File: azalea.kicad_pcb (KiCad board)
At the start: 4 copper layers, 70.6 x 53.3 mm, 103 parts, among them J1 NEIGHBOR1, J2 NEIGHBOR2, J3 USB-MICRO-B-SHIELDED, J4 USB-MICRO-B-SHIELDED, J5 JTAG, J6 POWER, J7 BONUS_ROW, SW1 DFU, SW2 RESET, U1 LPC4330FBD144, U2 W25Q16DV, U3 AP7333, U4 IP4220CZ6, U5 AP2553W6-7, X1 MCU_XTAL, X2 RTC_XTAL

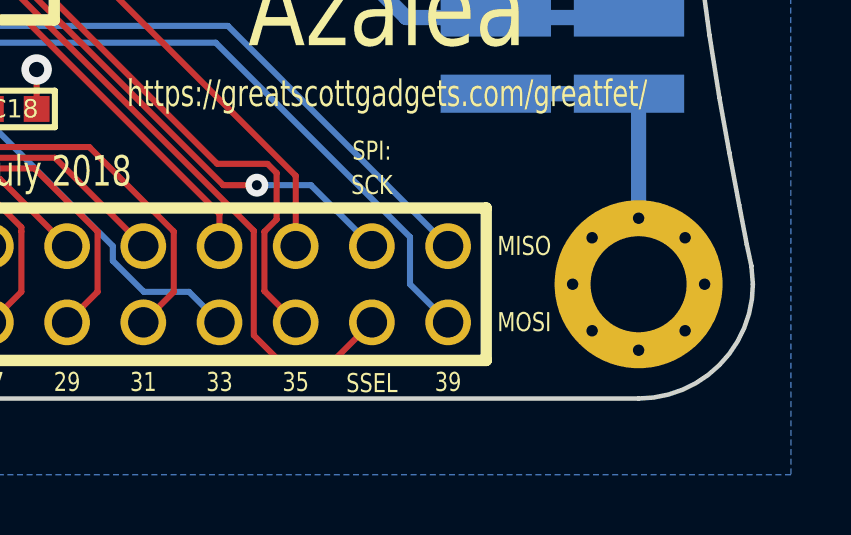
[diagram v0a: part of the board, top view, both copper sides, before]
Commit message: adopt OSHWA convention for SPI signal names https://www.oshwa.org/a-resolution-to-redefine-spi-signal-names
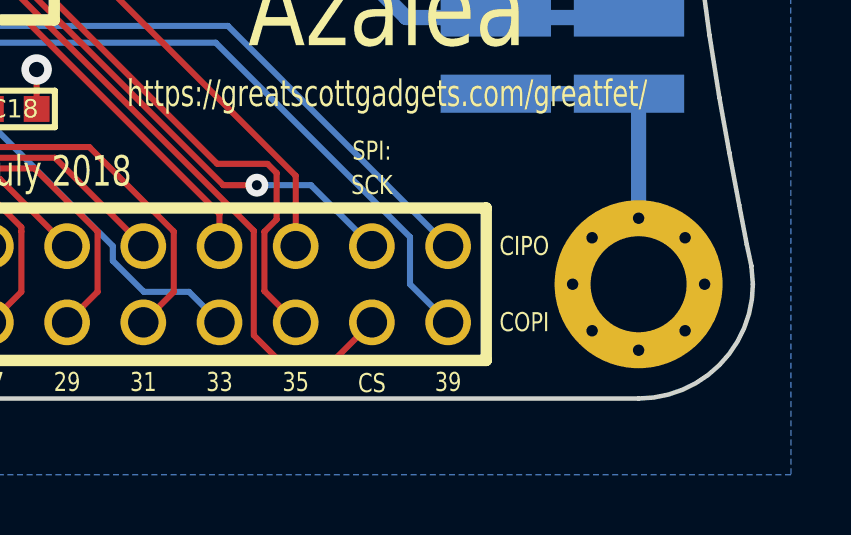
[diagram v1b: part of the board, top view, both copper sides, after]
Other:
- board text added: "CIPO"
- board text added: "COPI"
- board text added: "CS"
- board text removed: "MISO"
- board text removed: "MOSI"
- board text removed: "SSEL"
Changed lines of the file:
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@@
     (effects (font (size 0.635 0.508) (thickness 0.1016)) (justify mirror))
   )
-  (gr_text MOSI (at 168.91 121.92) (layer B.SilkS)
-    (effects (font (size 0.635 0.508) (thickness 0.1016)) (justify mirror))
-  )
-  (gr_text MISO (at 168.91 119.38) (layer B.SilkS)
+  (gr_text COPI (at 168.91 121.92) (layer B.SilkS)
+    (effects (font (size 0.635 0.508) (thickness 0.1016)) (justify mirror))
+  )
+  (gr_text CIPO (at 168.91 119.38) (layer B.SilkS)
     (effects (font (size 0.635 0.508) (thickness 0.1016)) (justify mirror))
   )
@@
     (effects (font (size 0.635 0.508) (thickness 0.1016)) (justify mirror))
   )
-  (gr_text SSEL (at 163.83 123.952) (layer B.SilkS)
+  (gr_text CS (at 163.83 123.952) (layer B.SilkS)
     (effects (font (size 0.635 0.508) (thickness 0.1016)) (justify mirror))
   )
@@
     (effects (font (size 0.635 0.508) (thickness 0.1016)))
   )
-  (gr_text SSEL (at 163.83 123.952) (layer F.SilkS)
-    (effects (font (size 0.635 0.508) (thickness 0.1016)))
-  )
-  (gr_text MISO (at 168.91 119.38) (layer F.SilkS)
-    (effects (font (size 0.635 0.508) (thickness 0.1016)))
-  )
-  (gr_text MOSI (at 168.91 121.92) (layer F.SilkS)
-    (effects (font (size 0.635 0.508) (thickness 0.1016)))
-  )
+  (gr_text CS (at 163.83 123.952) (layer F.SilkS)
+    (effects (font (size 0.635 0.508) (thickness 0.1016)))
+  )
+  (gr_text CIPO (at 168.91 119.38) (layer F.SilkS)
+    (effects (font (size 0.635 0.508) (thickness 0.1016)))
+  )
+  (gr_text COPI (at 168.91 121.92) (layer F.SilkS)
+    (effects (font (size 0.635 0.508) (thickness 0.1016)))
+  )

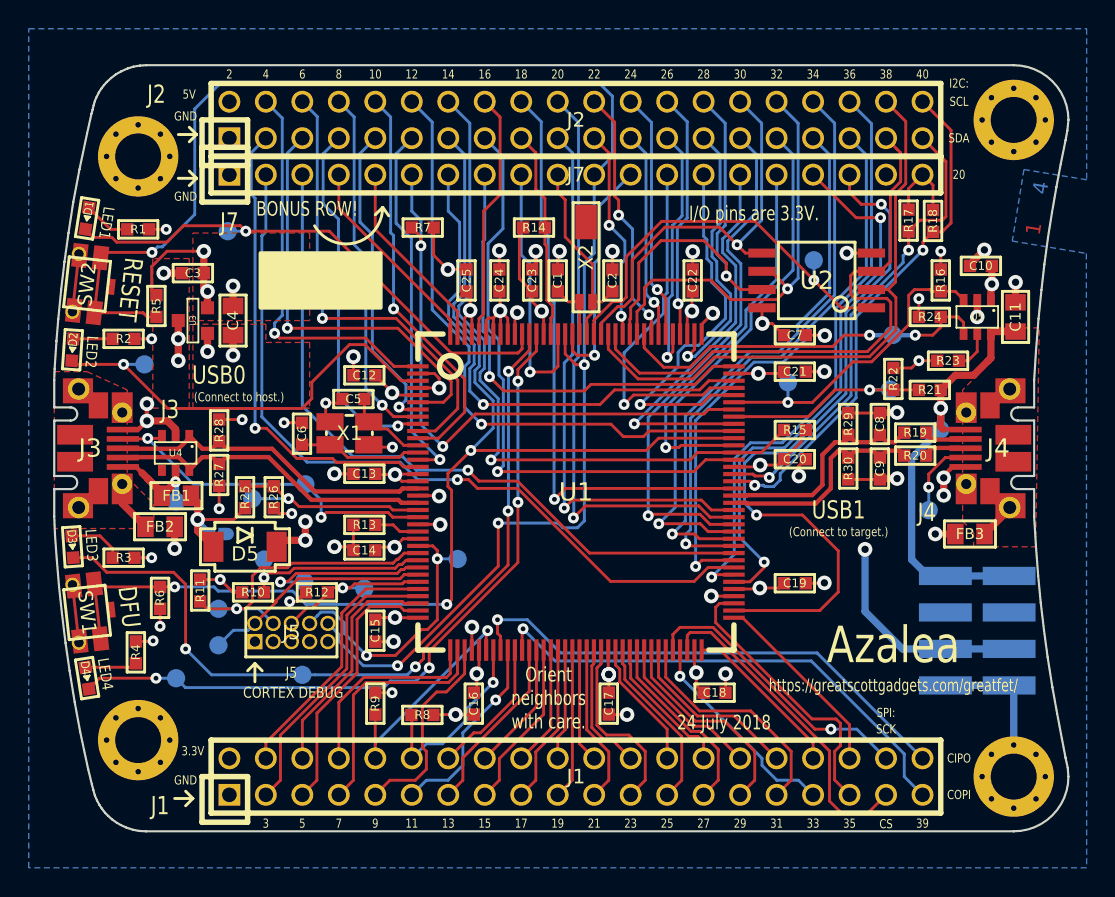
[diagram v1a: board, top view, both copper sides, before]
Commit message: GF1 hardware: Update PCB to reflect U5 & R23 peart changes.
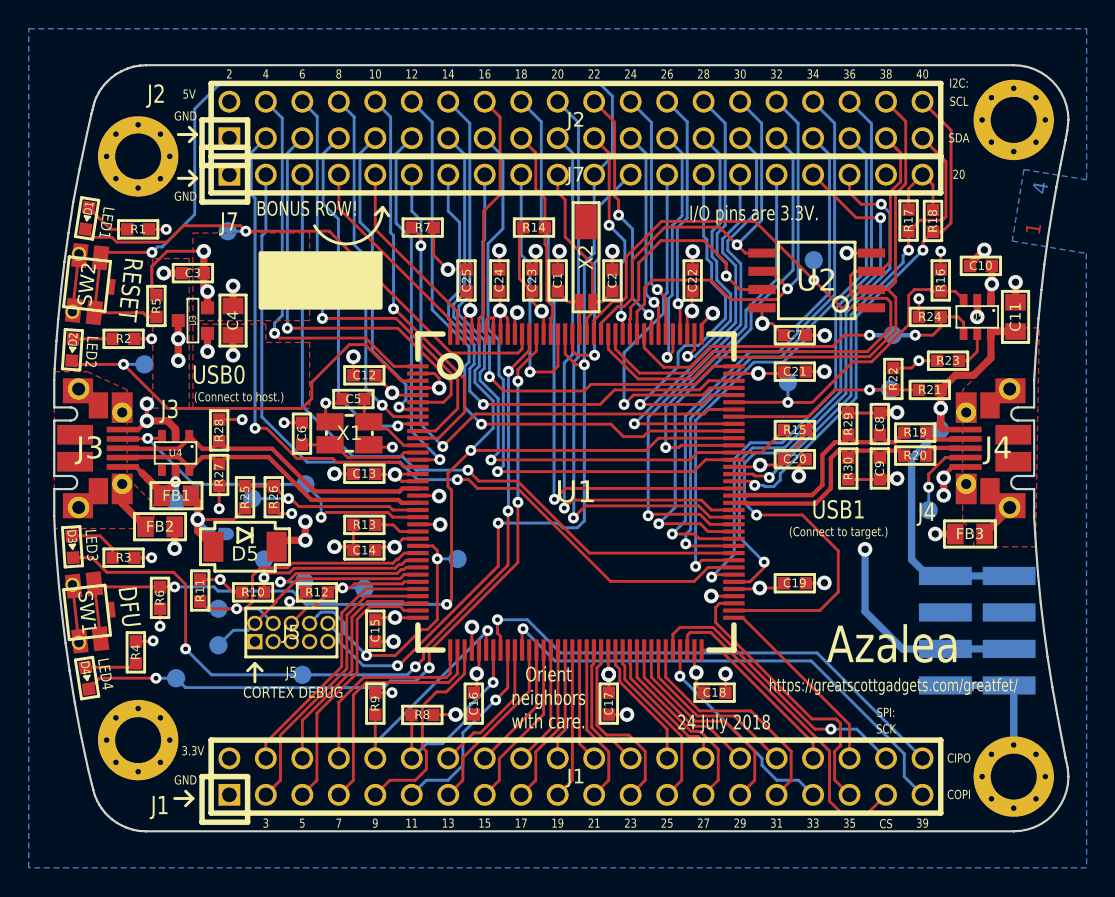
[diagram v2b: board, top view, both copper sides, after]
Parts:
- R23: value 43.2k -> 15k
- U5: value AP2553W6-7 -> AP22653AW6-7

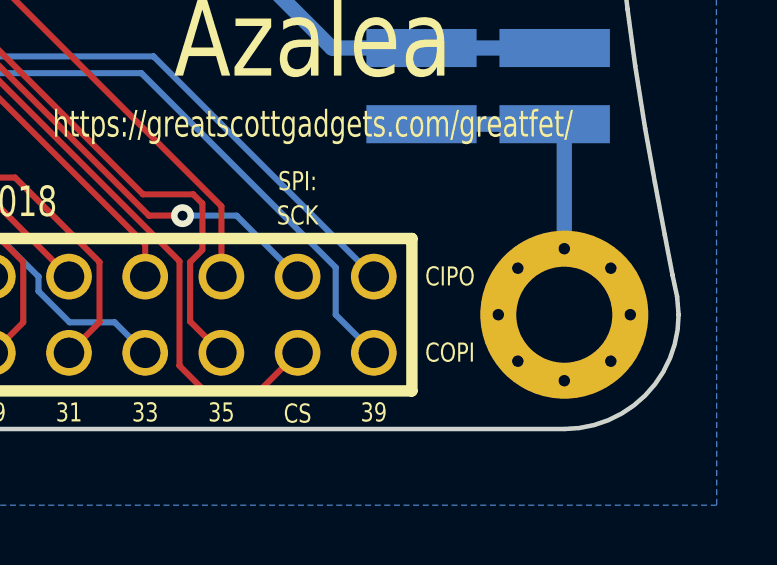
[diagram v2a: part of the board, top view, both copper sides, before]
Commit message: GF1 hardware: Update references from MOSI/MISO or COPI/CIPO to PICO/POCI
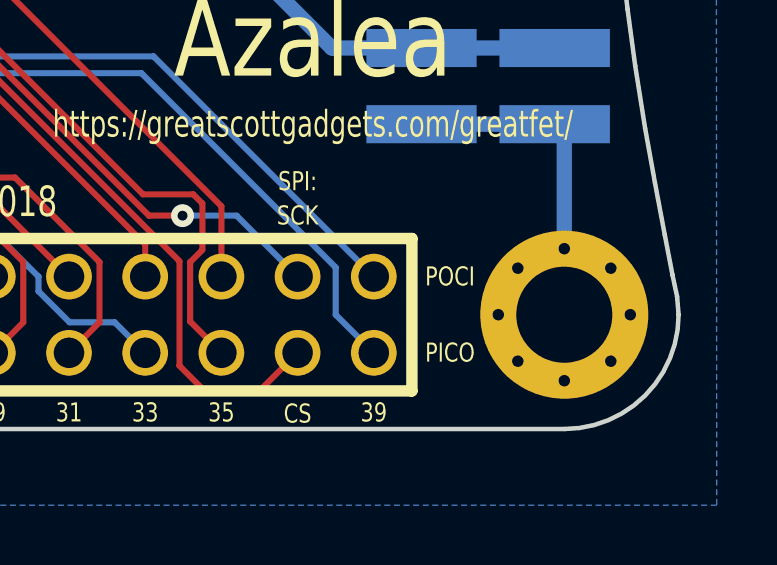
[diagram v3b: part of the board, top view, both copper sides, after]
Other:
- board text added: "PICO"
- board text added: "POCI"
- board text removed: "CIPO"
- board text removed: "COPI"

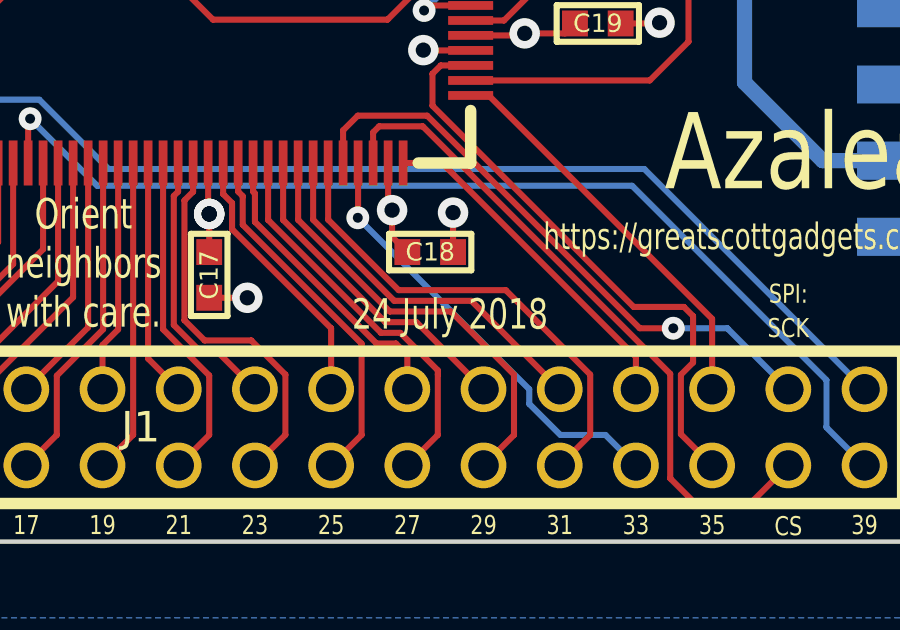
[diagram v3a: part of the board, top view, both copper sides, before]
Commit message: update date on silkscreen
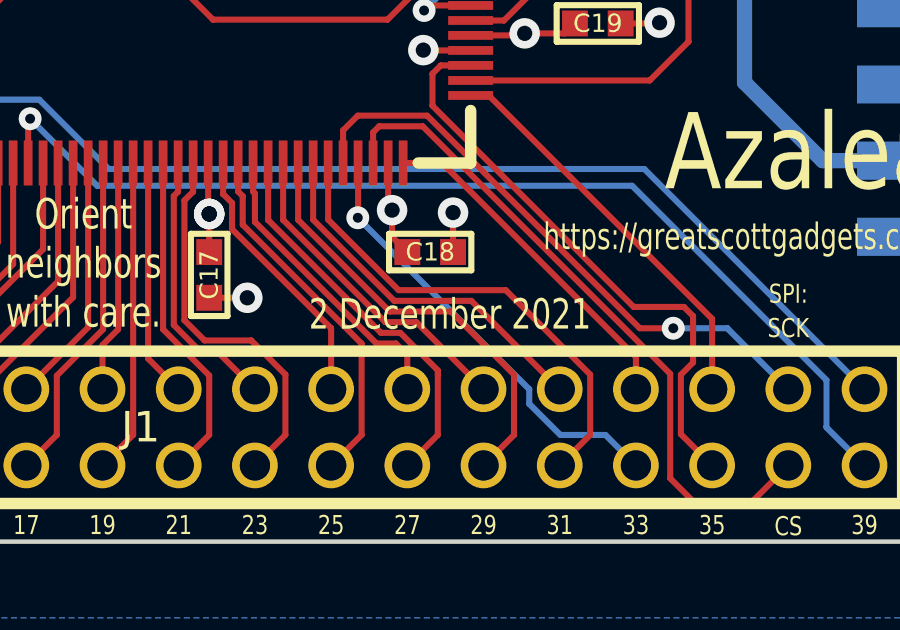
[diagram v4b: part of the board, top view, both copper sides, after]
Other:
- board text added: "2 December 2021"
- board text removed: "24 July 2018"
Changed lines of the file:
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@@
   (gr_line (start 128.778 81.026) (end 128.27 81.534) (angle 90) (layer F.SilkS) (width 0.15))
   (gr_arc (start 126.238 81.026) (end 128.778 81.026) (angle 150) (layer F.SilkS) (width 0.2032))
-  (gr_text "24 July 2018" (at 152.5524 116.8908) (layer F.SilkS)
+  (gr_text "2 December 2021" (at 152.5524 116.8908) (layer F.SilkS)
     (effects (font (size 1.016 0.762) (thickness 0.1524)))
   )
